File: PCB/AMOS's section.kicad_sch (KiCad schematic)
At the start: 7 parts, among them J2 Conn_02x16_Row_Letter_Last_Sh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, U8 BQ24074RGT

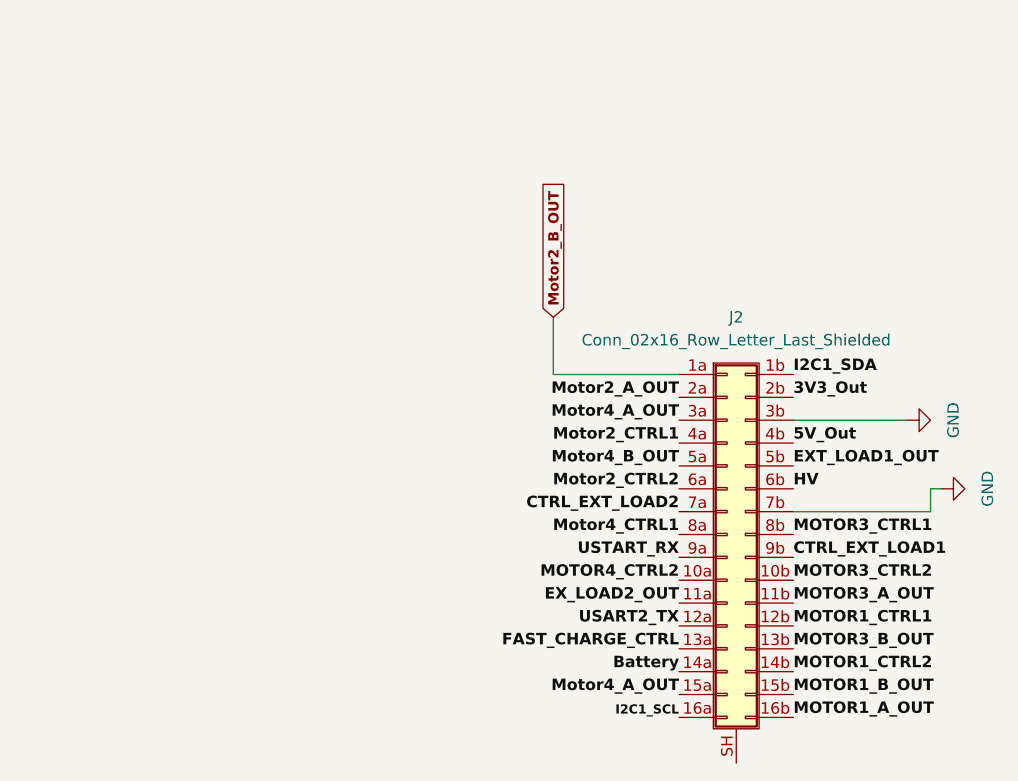
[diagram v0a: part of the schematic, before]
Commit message: Updated Voltage regulator circuit
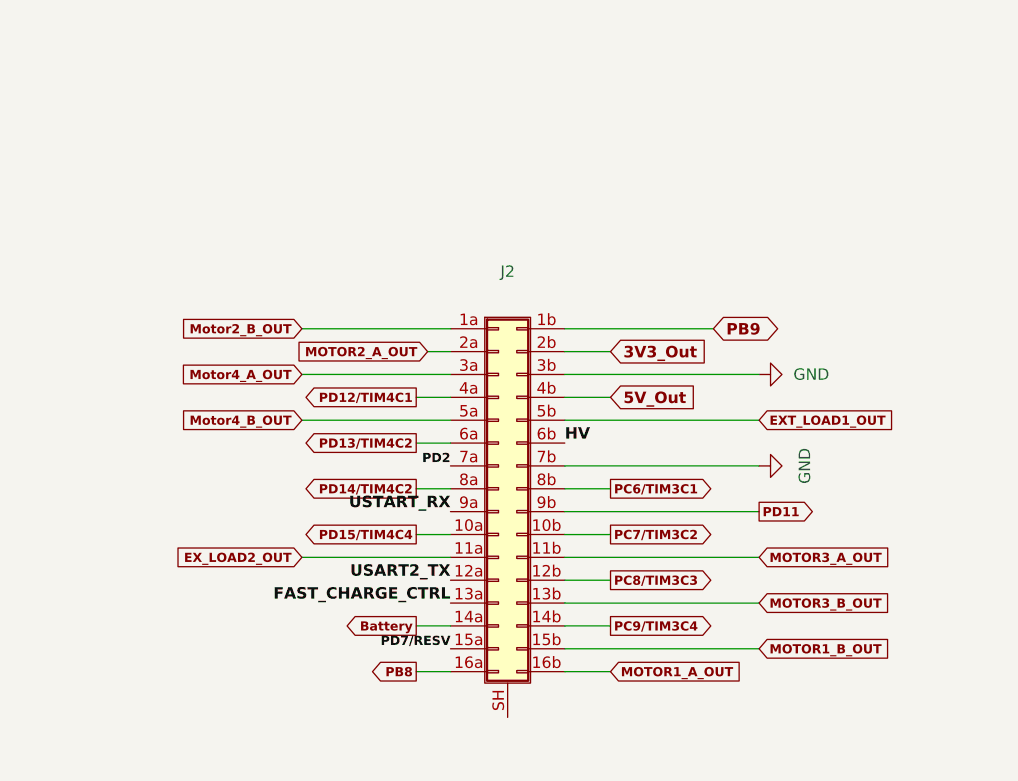
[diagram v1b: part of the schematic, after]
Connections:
- net Motor4_A_OUT: no longer J2.15a (Pin_15a)
- net CTRL_EXT_LOAD1 renamed PD11
- net CTRL_EXT_LOAD2 renamed PD2
- net I2C1_SCL renamed PB8
- net I2C1_SDA renamed PB9
- net MOTOR1_CTRL1 renamed PC8/TIM3C3
- net MOTOR1_CTRL2 renamed PC9/TIM3C4
- net MOTOR3_CTRL1 renamed PC6/TIM3C1
- net MOTOR3_CTRL2 renamed PC7/TIM3C2
- net MOTOR4_CTRL2 renamed PD15/TIM4C4
- net Motor2_A_OUT renamed MOTOR2_A_OUT
- net Motor2_CTRL1 renamed PD12/TIM4C1
- net Motor2_CTRL2 renamed PD13/TIM4C2
- net Motor4_CTRL1 renamed PD14/TIM4C2
- new net PD7/RESV: J2.15a (Pin_15a)
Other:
- moved on the sheet: J2

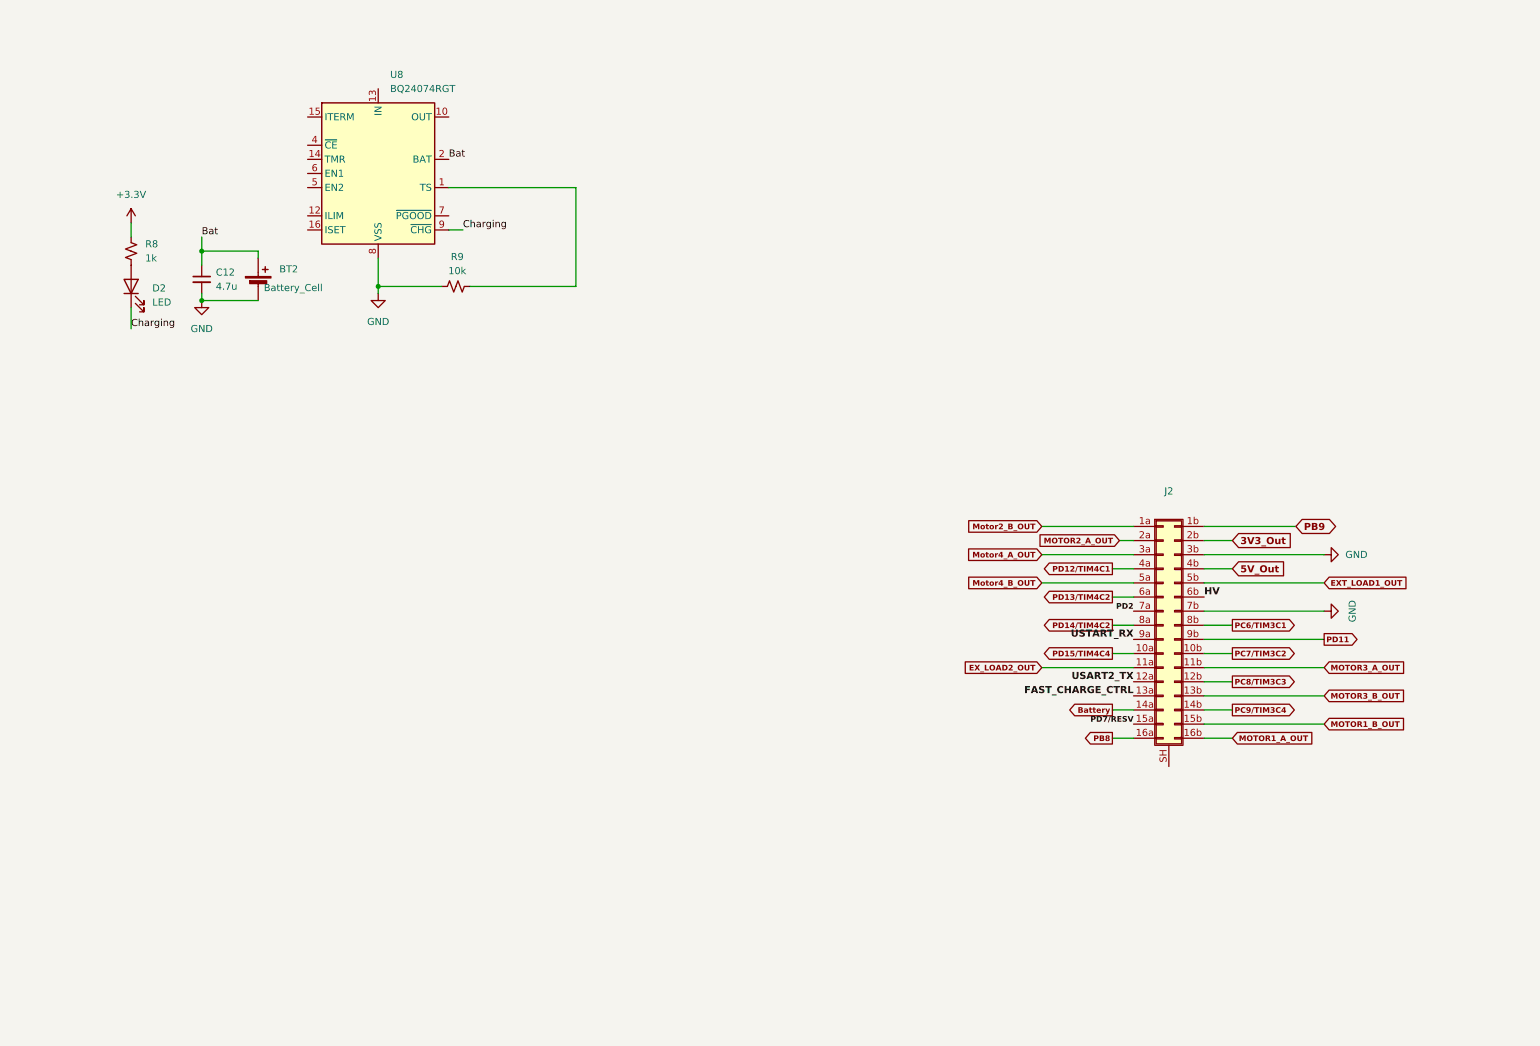
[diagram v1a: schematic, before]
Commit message: Add Chrarging circuit, USB integration, and pin headers
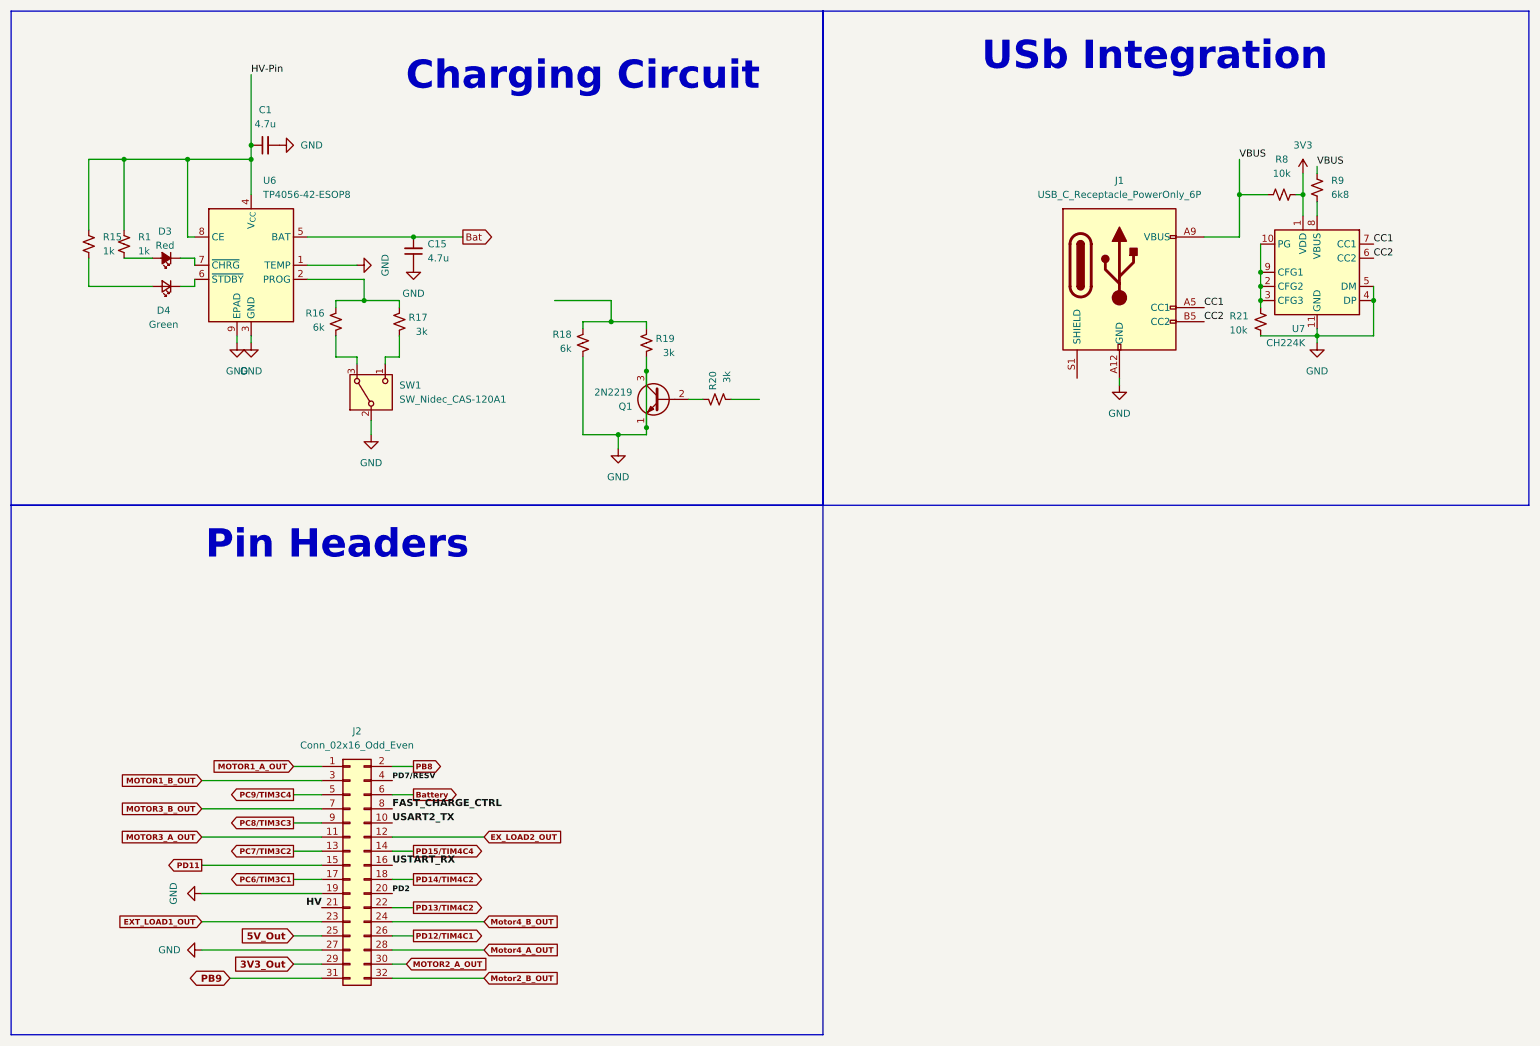
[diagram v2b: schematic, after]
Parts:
- removed BT2: Battery_Cell, symbol Device:Battery_Cell
- removed C12: 4.7u, symbol Device:C_Small
- removed D2: LED, symbol Device:LED
- removed J2: Conn_02x16_Row_Letter_Last_Shielded, symbol Connector_Generic_Shielded:Conn_02x16_Row_Letter_Last_Shielded
- removed U8: BQ24074RGT, Package_DFN_QFN:VQFN-16-1EP_3x3mm_P0.5mm_EP1.6x1.6mm, symbol Battery_Management:BQ24074RGT
- added C1, C15: 4.7u, symbol Device:C_Small
- added D3: Red, symbol Device:LED_Small_Filled
- added D4: Green, symbol Device:LED_Small
- added J1: USB_C_Receptacle_PowerOnly_6P, Connector_USB:USB_C_Receptacle_HCTL_HC-TYPE-C-16P-01A, symbol Connector:USB_C_Receptacle_PowerOnly_6P
- added J2: Conn_02x16_Odd_Even, symbol Connector_Generic:Conn_02x16_Odd_Even
- added Q1: 2N2219, Package_TO_SOT_THT:TO-39-3, symbol Transistor_BJT:2N2219
- added R1, R15: 1k, symbol Device:R_Small_US
- added R16, R18: 6k, symbol Device:R_Small_US
- added R17, R19, R20: 3k, symbol Device:R_Small_US
- added R21: 10k, symbol Device:R_Small_US
- added SW1: SW_Nidec_CAS-120A1, Button_Switch_SMD:Nidec_Copal_CAS-120A, symbol Switch:SW_Nidec_CAS-120A1
- added U6: TP4056-42-ESOP8, Package_SO:SOIC-8-1EP_3.9x4.9mm_P1.27mm_EP2.41x3.3mm_ThermalVias, symbol Battery_Management:TP4056-42-ESOP8
- added U7: CH224K, Package_SO:SSOP-10-1EP_3.9x4.9mm_P1mm_EP2.1x3.3mm, symbol Interface_USB:CH224K
- R8: value 1k -> 10k
- R9: value 10k -> 6k8
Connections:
- net +3.3V is gone; now on net VBUS: R8.1
- net 3V3_Out: now also J2.29 (Pin_29)
- net 5V_Out: now also J2.25 (Pin_25)
- net Bat: now also C15.2, U6.5 (BAT)
- net Battery: now also J2.6 (Pin_6)
- net EXT_LOAD1_OUT: now also J2.23 (Pin_23)
- net EX_LOAD2_OUT: now also J2.12 (Pin_12)
- net FAST_CHARGE_CTRL: now also J2.8 (Pin_8)
- net GND: now also C1.2, C15.1, J1.A12 (GND), J1.B12 (GND), J2.19 (Pin_19), J2.27 (Pin_27), Q1.1 (E), Q1.3 (C), R18.2, R19.2, R21.1, SW1.2 (B), U6.1 (TEMP), U6.3 (GND), U6.9 (EPAD), U7.11 (GND), U7.4 (DP), U7.5 (DM); no longer R9.1
- net HV: now also J2.21 (Pin_21)
- net MOTOR1_A_OUT: now also J2.1 (Pin_1)
- net MOTOR1_B_OUT: now also J2.3 (Pin_3)
- net MOTOR2_A_OUT: now also J2.30 (Pin_30)
- net MOTOR3_A_OUT: now also J2.11 (Pin_11)
- net MOTOR3_B_OUT: now also J2.7 (Pin_7)
- net Motor2_B_OUT: now also J2.32 (Pin_32)
- net Motor4_A_OUT: now also J2.28 (Pin_28)
- net Motor4_B_OUT: now also J2.24 (Pin_24)
- net PB8: now also J2.2 (Pin_2)
- net PB9: now also J2.31 (Pin_31)
- net PC6/TIM3C1: now also J2.17 (Pin_17)
- net PC7/TIM3C2: now also J2.13 (Pin_13)
- net PC8/TIM3C3: now also J2.9 (Pin_9)
- net PC9/TIM3C4: now also J2.5 (Pin_5)
- net PD11: now also J2.15 (Pin_15)
- net PD12/TIM4C1: now also J2.26 (Pin_26)
- net PD13/TIM4C2: now also J2.22 (Pin_22)
- net PD14/TIM4C2: now also J2.18 (Pin_18)
- net PD15/TIM4C4: now also J2.14 (Pin_14)
- net PD2: now also J2.20 (Pin_20)
- net PD7/RESV: now also J2.4 (Pin_4)
- net USART2_TX: now also J2.10 (Pin_10)
- net USTART_RX: now also J2.16 (Pin_16)
- net 3V3: now reaches R8.2
- net 3V3: now also U7.1 (VDD)
- net VBUS: now reaches R9.2
- net VBUS: now also J1.A9 (VBUS), J1.B9 (VBUS)
- new net: R21.2, U7.10 (PG), U7.2 (CFG2), U7.3 (CFG3), U7.9 (CFG1)
- new net: R9.1, U7.8 (VBUS)
- new net: D3.1 (K), U6.7 (~{CHRG})
- new net: D3.2 (A), R1.2
- new net: R16.1, R17.1, U6.2 (PROG)
- new net: D4.1 (K), U6.6 (~{STDBY})
- new net: R18.1, R19.1
- new net: R17.2, SW1.1 (C)
- new net: R16.2, SW1.3 (A)
- new net: D4.2 (A), R15.2
- new net: Q1.2 (B), R20.1
- new net CC1: J1.A5 (CC1), U7.7 (CC1)
- new net CC2: J1.B5 (CC2), U7.6 (CC2)
- new net HV-Pin: C1.1, R1.1, R15.1, U6.4 (V_{CC}), U6.8 (CE)
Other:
- note added: "Charging Circuit"
- note added: "Pin Headers"
- note added: "USb Integration"
